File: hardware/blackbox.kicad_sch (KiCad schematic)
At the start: 3 parts

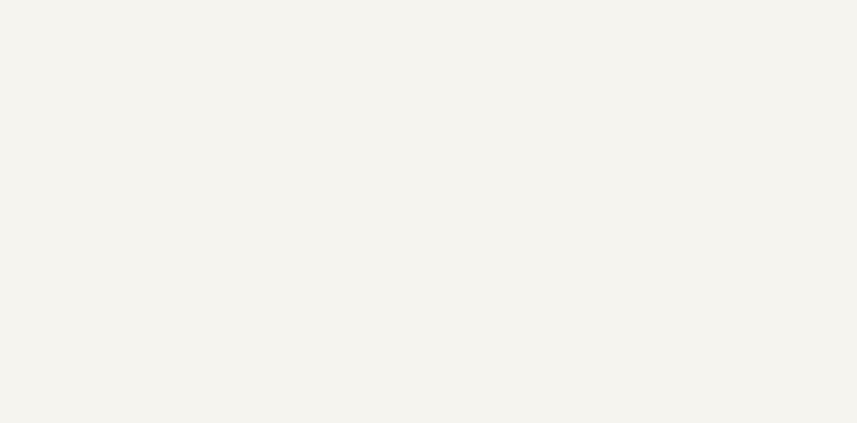
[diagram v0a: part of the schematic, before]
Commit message: Rev 2: finalize schematic + PCB for fabrication
Rev 2 change list implemented; on-canvas design annotations added across all
sheets (root, rp2350a, power, imu, osd, blackbox, pads). Design frozen for ordering.

Co-Authored-By: Claude Opus 4.8 (1M context) <noreply@anthropic.com>
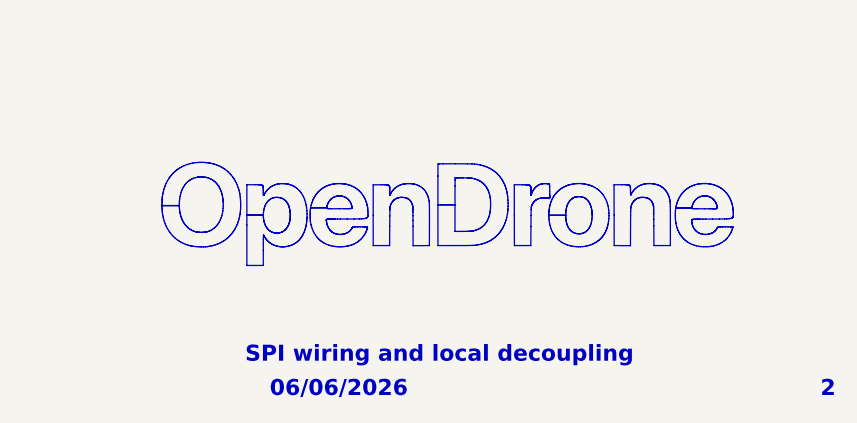
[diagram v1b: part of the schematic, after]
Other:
- note added: "06/06/2026"
- note added: "2"
- note added: "SPI wiring and local decoupling"

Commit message: chore(bom): consolidate LCSC Part -> LCSC field across schematic, library, footprints, project
Single canonical LCSC field (was split LCSC / LCSC Part). Every part resolves to one LCSC code; netlist verified, no duplicates. Includes Rev2 re-annotation resync re-save.

Co-Authored-By: Claude Opus 4.8 (1M context) <noreply@anthropic.com>
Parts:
- Card1: LCSC (none) -> C393941; LCSC Part C393941 -> (none)
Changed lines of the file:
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@@
 			)
 		)
-		(property "LCSC Part" "C393941"
+		(property "LCSC" "C393941"
 			(at 60.96 41.91 0)
 			(hide yes)
